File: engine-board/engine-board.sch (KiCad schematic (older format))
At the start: 17 parts, among them J101 SD Card, U101 Teensy3.6_All_Pins, U102 FEATHER_M0_BASIC_PROTO

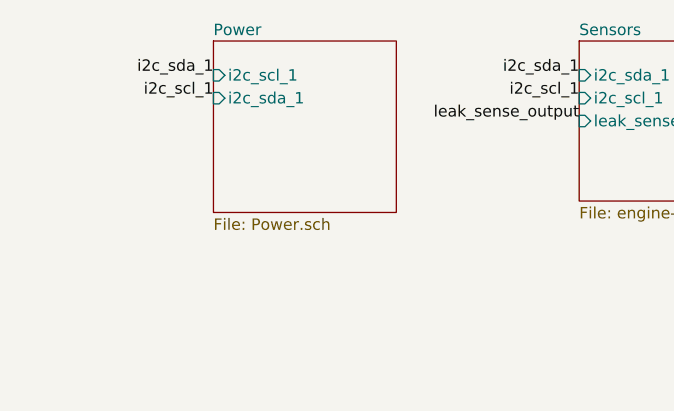
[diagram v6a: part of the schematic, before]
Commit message: ready for layout
- added batt solder tabs
- swapped some terminal blocks with microfit connectors
- shortened board, tightened layout
- tried to space everything out properly
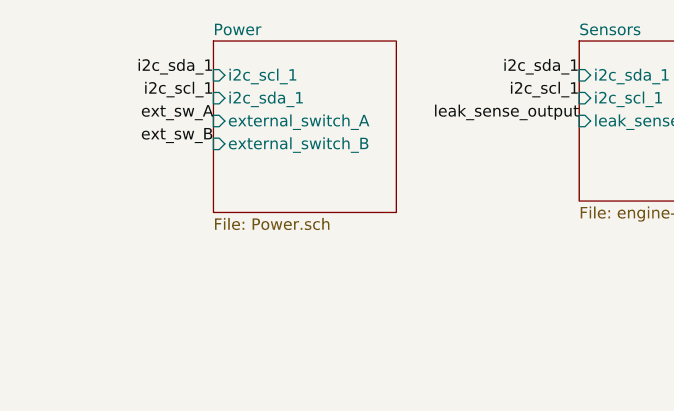
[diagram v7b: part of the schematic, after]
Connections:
- net labels added: ext_sw_A, ext_sw_B
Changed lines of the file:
@@
 F2 "i2c_scl_1" I L 1200 750 50
 F3 "i2c_sda_1" I L 1200 850 50
+F4 "external_switch_A" I L 1200 950 50
+F5 "external_switch_B" I L 1200 1050 50
 $EndSheet
 $Sheet
@@
 Text Label 4600 800  2    50   ~ 0
 usb_data_D1
+Text Label 1200 950  2    50   ~ 0
+ext_sw_A
+Text Label 1200 1050 2    50   ~ 0
+ext_sw_B
 $EndSCHEMATC

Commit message: ready for routing
- figured out battery input - going with solder strips + sense wires to reduce connector count
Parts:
- U101: symbol teensy:Teensy3.6_All_Pins -> engine-board-rescue:Teensy3.6_All_Pins-teensy
- U102: symbol engine-board-rescue:FEATHER_M0_BASIC_PROTO-FEATHER_M0_BASIC_PROTO-engine-board-rescue -> engine-board-rescue:FEATHER_M0_BASIC_PROTO-FEATHER_M0_BASIC_PROTO-engine-board-rescue-engine-board-rescue
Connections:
- net labels added: rs232_gnd, rs232_rx, rs232_tx
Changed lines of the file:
@@
 $EndComp
 $Comp
-L engine-board-rescue:FEATHER_M0_BASIC_PROTO-FEATHER_M0_BASIC_PROTO-engine-board-rescue U102
+L engine-board-rescue:FEATHER_M0_BASIC_PROTO-FEATHER_M0_BASIC_PROTO-engine-board-rescue-engine-board-rescue U102
 U 1 1 60CE6FB5
 P 7700 5550
@@
 F3 "i2c_scl_1" I L 2800 850 50
 F4 "leak_sense_output" I L 2800 950 50
+F5 "ext_SWA" I L 2800 1050 50
+F6 "ext_SWB" I L 2800 1150 50
 $EndSheet
 $Sheet
@@
 $EndSheet
 $Sheet
-S 1200 600  800  750
+S 1200 600  800  1000
 U 61B60659
 F0 "Power" 50
@@
 F4 "external_switch_A" I L 1200 950 50
 F5 "external_switch_B" I L 1200 1050 50
+F6 "rs232_tx" I L 1200 1150 50
+F7 "rs232_rx" I L 1200 1250 50
+F8 "rs232_gnd" I L 1200 1350 50
+F9 "usb_D0" I L 1200 1450 50
+F10 "usb_D1" I L 1200 1550 50
 $EndSheet
 $Sheet
@@
 i2c_sda_1
 $Comp
-L teensy:Teensy3.6_All_Pins U101
+L engine-board-rescue:Teensy3.6_All_Pins-teensy U101
 U 1 1 61A700C3
 P 2750 5200
@@
 L power:GND #PWR0103
 U 1 1 61AFF33A
-P 1200 3050
-F 0 "#PWR0103" H 1200 2800 50  0001 C CNN
-F 1 "GND" H 1205 2877 50  0000 C CNN
-F 2 "" H 1200 3050 50  0001 C CNN
-F 3 "" H 1200 3050 50  0001 C CNN
-	1    1200 3050
-	1    0    0    -1
-$EndComp
-Wire Wire Line
-	1600 3050 1200 3050
+P 850 3050
+F 0 "#PWR0103" H 850 2800 50  0001 C CNN
+F 1 "GND" H 855 2877 50  0000 C CNN
+F 2 "" H 850 3050 50  0001 C CNN
+F 3 "" H 850 3050 50  0001 C CNN
+	1    850  3050
+	1    0    0    -1
+$EndComp
 Text Label 1600 4850 2    50   ~ 0
 irid_TXD
@@
 Wire Wire Line
 	5900 6350 5900 6300
-Text Label 4600 700  2    50   ~ 0
+Text Label 1200 1450 2    50   ~ 0
 usb_data_D0
-Text Label 4600 800  2    50   ~ 0
+Text Label 1200 1550 2    50   ~ 0
 usb_data_D1
 Text Label 1200 950  2    50   ~ 0
@@
 Text Label 1200 1050 2    50   ~ 0
 ext_sw_B
+Text Label 2800 1050 2    50   ~ 0
+ext_sw_A
+Text Label 2800 1150 2    50   ~ 0
+ext_sw_B
+Wire Wire Line
+	1600 3050 850  3050
+Text Label 1200 1150 2    50   ~ 0
+rs232_tx
+Text Label 1600 3250 2    50   ~ 0
+rs232_tx
+Text Label 1200 1250 2    50   ~ 0
+rs232_rx
+Text Label 1600 3150 2    50   ~ 0
+rs232_rx
+Text Label 1200 1350 2    50   ~ 0
+rs232_gnd
+Text Label 850  3050 2    50   ~ 0
+rs232_gnd
 $EndSCHEMATC
